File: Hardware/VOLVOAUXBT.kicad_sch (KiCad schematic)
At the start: 81 parts, among them J1 10118193-0001LF, J10 Conn_01x02_Pin, J11 Conn_01x02_Pin, J12 Conn_01x05_Pin, J13 Conn_01x05_Pin, J14 Conn_01x05_Pin, J15 Conn_01x02_Pin, J16 Conn_01x02_Pin, J17 Conn_01x01_Pin, J18 Conn_01x02_Pin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

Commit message: First iteration of PCB routing
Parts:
- removed C10: 1uF/16V(10%), Capacitor_SMD:C_1206_3216Metric, symbol Device:C
- removed C11: 10uF/25V(20%), Capacitor_SMD:C_1206_3216Metric, symbol Device:C
- removed C14: 0.1uF/50V(10%), Capacitor_SMD:C_1206_3216Metric, symbol Device:C
- removed J12, J13: Conn_01x05_Pin, Connector_PinHeader_2.54mm:PinHeader_1x05_P2.54mm_Vertical, symbol Connector:Conn_01x05_Pin
- removed R10, R19, R22, R24, R5, R6, R7, R8, R9: 500, Resistor_SMD:R_0603_1608Metric, symbol Device:R
- removed U4: ESP32-MINI-1, PCM_Espressif:ESP32-MINI-1, symbol PCM_Espressif:ESP32-MINI-1
- R4: value 10K(1%) -> 500
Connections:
- net CD_GND is gone; now on net GND: J3.14, J3.2, J4.17 (Pin_17), J4.5 (Pin_5), J5.17 (Pin_17), J5.5 (Pin_5)
- net MB_GND is gone; now on net GND: J6.17, J6.5, J7.17 (Pin_17), J7.5 (Pin_5)
- net BTM_GPIO_R1: no longer R3.1
- net BTM_GPIO_R2: no longer R1.1
- net BTM_ON/OFF: now also R3.1
- net BTM_PLAY: now also R4.1
- net BTM_USB_VBUS: now also U6.16 (VCC)
- net BTM_VOL+: now also R1.1
- net CD_I2S_LRCK: no longer J5.1 (Pin_1)
- net ESP_RST: no longer R4.2
- net LIN1_RXD: now also U8.26 (ADC2_CH0/GPIO4); no longer U8.11 (DAC_2/ADC2_CH9/GPIO26)
- net LIN1_SLP: now also U8.37 (GPIO23); no longer U8.9 (32K_XN/GPIO33/ADC1_CH5)
- net LIN1_TXD: now also U8.28 (GPIO17); no longer U8.12 (ADC2_CH7/GPIO27)
- net LIN2_RXD: now also U8.36 (GPIO22); no longer U8.31 (GPIO19)
- net LIN2_SLP: now also U8.31 (GPIO19); no longer U8.8 (32K_XP/GPIO32/ADC1_CH4)
- net MUX_CONT: now also U8.12 (ADC2_CH7/GPIO27); no longer U8.26 (ADC2_CH0/GPIO4)
- net VBUS: no longer U6.16 (VCC)
- net VCC_3V3: no longer R4.1
- net at R3.2: now also U8.8 (32K_XP/GPIO32/ADC1_CH4)
- net at R1.2: now also U8.11 (DAC_2/ADC2_CH9/GPIO26)
- new net: R4.2, U8.9 (32K_XN/GPIO33/ADC1_CH5)
- no-connect marks 42 -> 37

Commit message: Crappy routing, too cramped
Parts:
- removed C19: 10uF/25V(20%), Capacitor_SMD:C_1206_3216Metric, symbol Device:C
- removed C22: 1uF/16V, Capacitor_SMD:C_1206_3216Metric, symbol Device:C
- removed R11: 1K, Resistor_SMD:R_0603_1608Metric, symbol Device:R
- removed R13: 22.1K, Resistor_SMD:R_0603_1608Metric, symbol Device:R
- removed R14: 47.5K, Resistor_SMD:R_0603_1608Metric, symbol Device:R
- removed R15: 10k(NC), Resistor_SMD:R_0603_1608Metric, symbol Device:R
- removed U7: CP2102N-Axx-xQFN20, Package_DFN_QFN:SiliconLabs_QFN-20-1EP_3x3mm_P0.5mm_EP1.8x1.8mm_ThermalVias, symbol Interface_USB:CP2102N-Axx-xQFN20
- added C10, C11: 0.1uF/25V(20%), Capacitor_SMD:C_1206_3216Metric, symbol Device:C
- added U4: CH340N, Package_SO:SOP-8_3.9x4.9mm_P1.27mm, symbol CH340:CH340N
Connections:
- net CD_I2S_LRCK: now also J5.1 (Pin_1)
- net GND: now also C10.1, C11.2, U4.3 (GND)
- net U0RXD: now also U4.6 (TXD)
- net U0TXD: now also U4.7 (RXD)
- net USB_DN: now also U4.2 (UD-)
- net USB_DP: now also U4.1 (UD+)
- net VBUS: now also C10.2, U4.5 (VCC)
- new net: C11.1, U4.8 (V3)
- no-connect marks 37 -> 30

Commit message: Routing with low side clearence. Pending accurate measurments for produciton
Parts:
- removed J15: Conn_01x02_Pin, Connector_PinHeader_2.54mm:PinHeader_1x02_P2.54mm_Vertical, symbol Connector:Conn_01x02_Pin
- removed J17, J19: Conn_01x01_Pin, Connector_PinHeader_2.54mm:PinHeader_1x01_P2.54mm_Vertical, symbol Connector:Conn_01x01_Pin
- removed J20, J21: Conn_01x05_Pin, Connector_PinHeader_2.54mm:PinHeader_1x05_P2.54mm_Vertical, symbol Connector:Conn_01x05_Pin
- added J12: Conn_01x02_Pin, Connector_PinHeader_2.54mm:PinHeader_1x02_P2.54mm_Vertical, symbol Connector:Conn_01x02_Pin
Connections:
- net BTM_NEXT: now also R3.1; no longer R20.1
- net BTM_ON/OFF: now also R20.1; no longer R3.1
- net BTM_USB_VBUS: no longer C1.1, C2.1, U1.3 (VI), U6.16 (VCC)
- net CD_ACC-ON: now also J12.2 (Pin_2)
- net ESP_RST: now also C23.1, J10.2 (Pin_2), R16.2, U8.3 (EN/CHIP_PU); no longer J9.1 (Pin_1)
- net EXT_5V: no longer J16.2 (Pin_2)
- net GND: now also J9.2 (Pin_2); no longer J10.2 (Pin_2)
- net GPIO0: now also J9.1 (Pin_1); no longer J9.2 (Pin_2)
- net LIN1: now also J14.4 (Pin_4); no longer J14.3 (Pin_3)
- net LIN1_RXD: now also U8.30 (GPIO18); no longer U8.26 (ADC2_CH0/GPIO4)
- net LIN1_SLP: now also U8.28 (GPIO17); no longer U8.37 (GPIO23)
- net LIN1_TXD: now also U8.26 (ADC2_CH0/GPIO4); no longer U8.28 (GPIO17)
- net LIN2: now also J14.3 (Pin_3); no longer J14.4 (Pin_4)
- net LIN2_RXD: now also U8.37 (GPIO23); no longer U8.36 (GPIO22)
- net LIN2_SLP: now also U8.36 (GPIO22); no longer U8.31 (GPIO19)
- net LIN2_TXD: now also U8.31 (GPIO19); no longer U8.30 (GPIO18)
- net VBUS: now also C1.1, C2.1, J16.2 (Pin_2), U1.3 (VI), U6.16 (VCC)
- net at U6.14 (4A): now also J12.1 (Pin_1)
- no-connect marks 30 -> 34

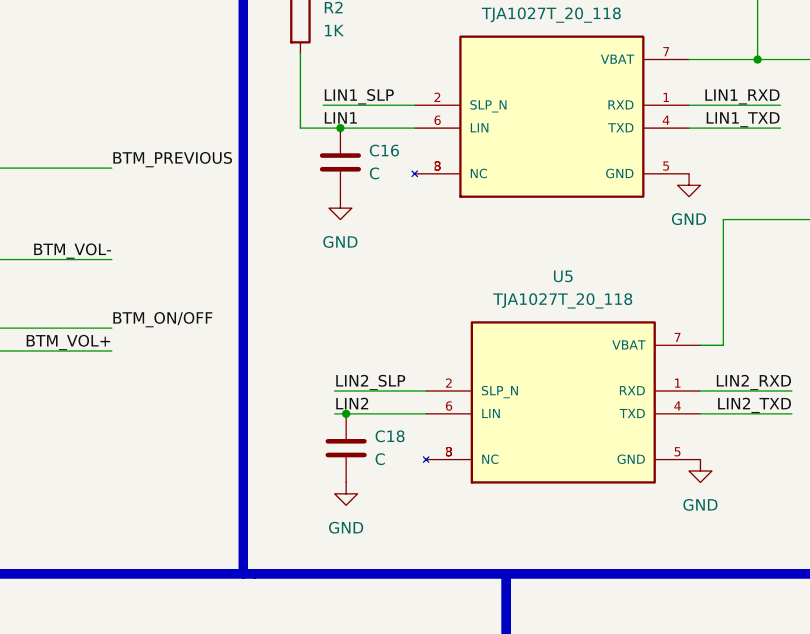
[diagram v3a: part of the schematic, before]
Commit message: XST set to 2.5mm. Swapping for 2.54mm
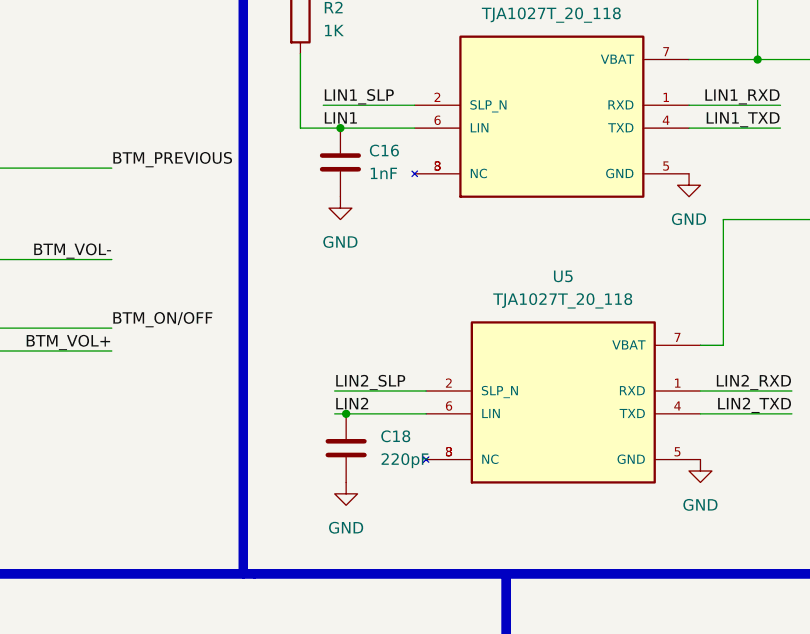
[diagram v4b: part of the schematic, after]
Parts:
- C16: value C -> 1nF
- C18: value C -> 220pF
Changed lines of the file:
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@@
       (effects (font (size 1.27 1.27)) (justify left))
     )
-    (property "Value" "C" (at 322.58 134.62 0)
+    (property "Value" "1nF" (at 322.58 134.62 0)
       (effects (font (size 1.27 1.27)) (justify left))
     )
@@
   (symbol (lib_id "Device:C") (at 320.04 165.1 0) (unit 1)
     (in_bom yes) (on_board yes) (dnp no) (fields_autoplaced)
-    (property "Reference" "C18" (at 323.215 163.83 0)
-      (effects (font (size 1.27 1.27)) (justify left))
-    )
-    (property "Value" "C" (at 323.215 166.37 0)
-      (effects (font (size 1.27 1.27)) (justify left))
-    )
+    (property "Reference" "C18" (at 323.85 163.83 0)
+      (effects (font (size 1.27 1.27)) (justify left))
+    )
+    (property "Value" "220pF" (at 323.85 166.37 0)
+      (effects (font (size 1.27 1.27)) (justify left))
+    )
